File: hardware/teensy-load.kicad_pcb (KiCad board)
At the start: 2 copper layers, 43.2 x 59.1 mm, 19 parts, among them J101 Conn_01x02, J201 Conn_01x01_Male, Q201 BTS141, U101 TEENSY_4.0, U102 TLV4333, U201 DAC6571, U301 DAC6571

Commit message: After footprint check, before layout
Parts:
- added R201: 10K, Resistor_SMD:R_0805_2012Metric_Pad1.15x1.40mm_HandSolder, F.Cu at (118.7, 120.4)
- added R206: 10K, Resistor_SMD:R_0805_2012Metric_Pad1.15x1.40mm_HandSolder, F.Cu at (118.7, 123.3)
- added R207: 22K, Resistor_SMD:R_0805_2012Metric_Pad1.15x1.40mm_HandSolder, F.Cu at (123.5, 120.4)
- added R208: 220K, Resistor_SMD:R_0805_2012Metric_Pad1.15x1.40mm_HandSolder, F.Cu at (136.2, 114.6)
- added R303: 33K, Resistor_SMD:R_0805_2012Metric_Pad1.15x1.40mm_HandSolder, F.Cu at (133.2, 120.4)
- added R304: 27K, Resistor_SMD:R_0805_2012Metric_Pad1.15x1.40mm_HandSolder, F.Cu at (144.8, 114.6)
- added R305: 33K, Resistor_SMD:R_0805_2012Metric_Pad1.15x1.40mm_HandSolder, F.Cu at (138.0, 120.4)
- added R306: 39K, Resistor_SMD:R_0805_2012Metric_Pad1.15x1.40mm_HandSolder, F.Cu at (149.5, 114.6)
- R202: renamed from R201; value 23K -> 220K
- R203: renamed from R202; value 10K -> 22K
- R205: renamed from R204; value 0.1, 1W -> 10m, 3W
- R301: value 10K -> 39K
- R302: value 15K -> 27K
- R307: renamed from R303; value 9K -> 18K
- R308: renamed from R304; value 1K -> 2K
- moved J101 41.2 mm to (130.8, 45.1), turned to 180 degrees
- moved R205 5.24 mm to (135.9, 75.6), turned to 180 degrees
- renumbered R203 to R204
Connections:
- R302 pad 2: GND -> Net-(R302-Pad2)
- U102 pad 13: /Voltage control/V_SENSE -> Net-(R304-Pad1)
- U102 pad 6: /Current control/I_SENSE -> Net-(R206-Pad1)

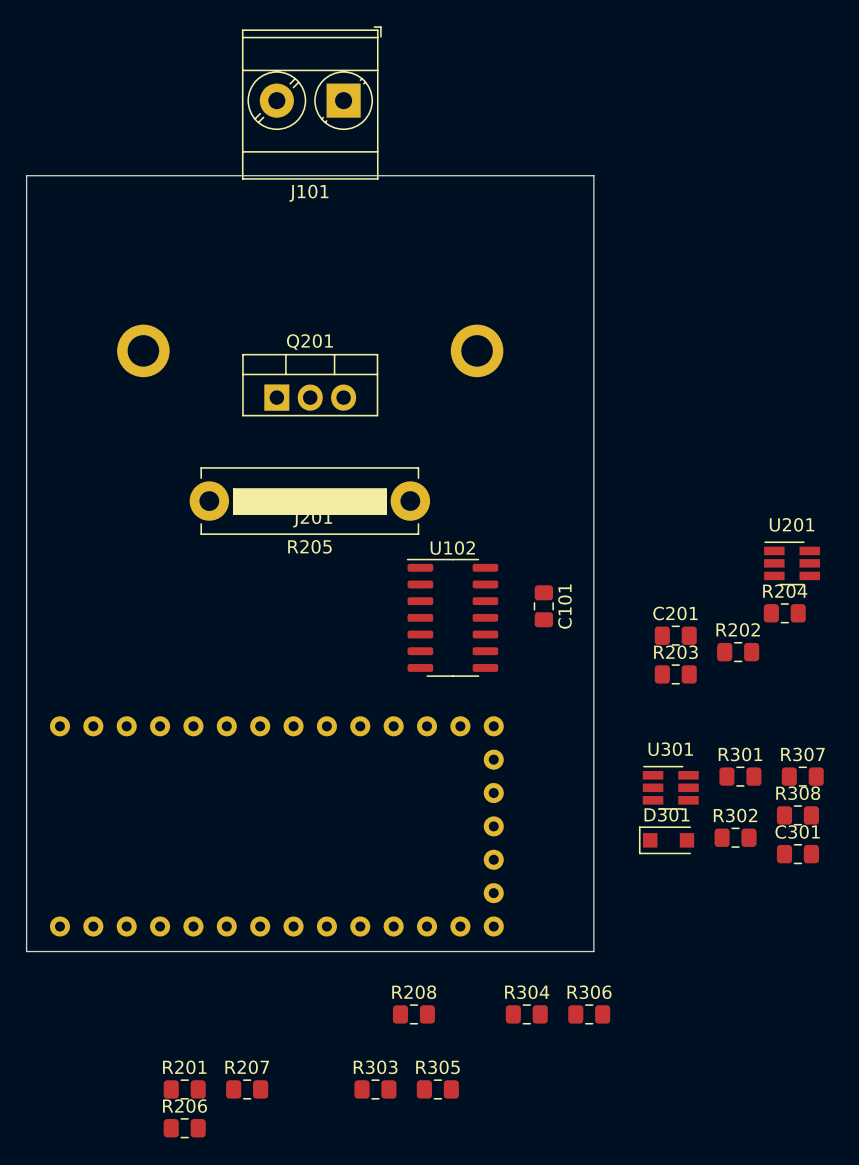
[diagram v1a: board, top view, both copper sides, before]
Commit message: Initial component placement
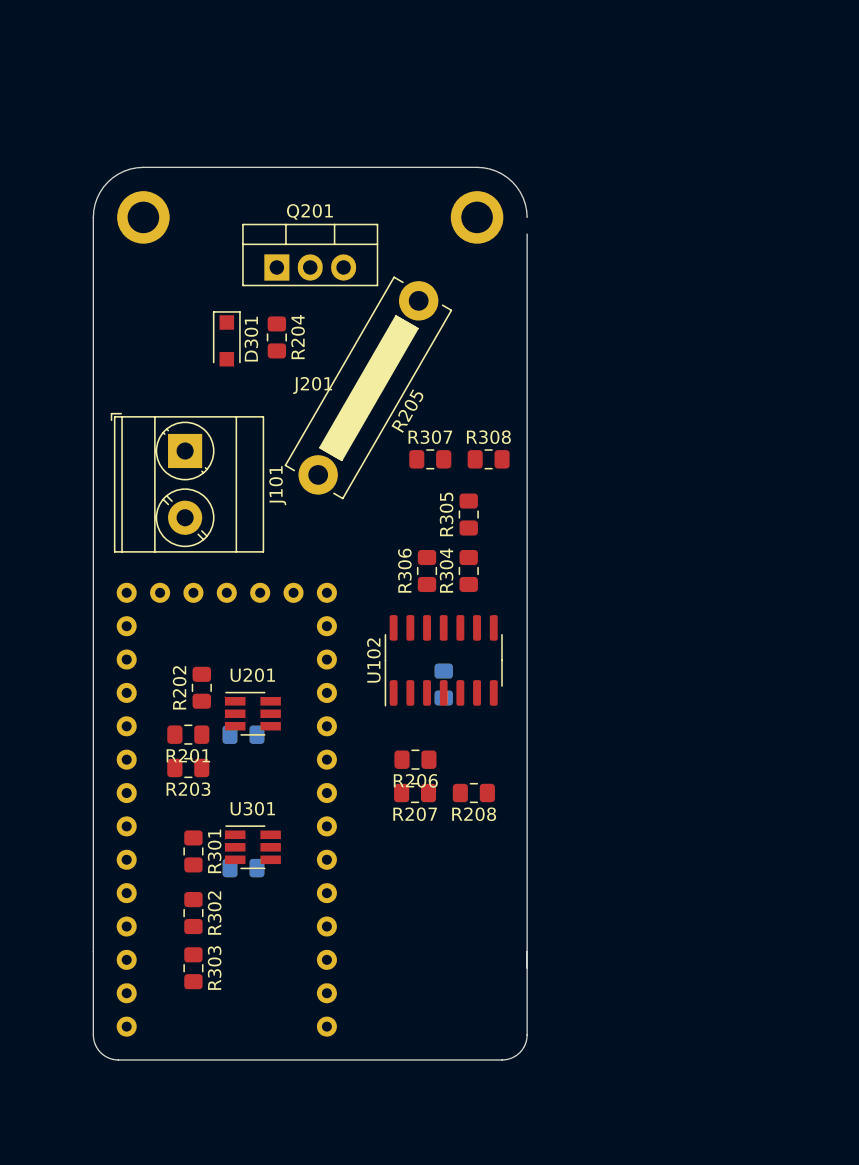
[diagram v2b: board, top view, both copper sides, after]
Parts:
- C101, C201, C301: moved to B.Cu
- moved D301 50.8 mm to (121.9, 63.4), turned to 270 degrees
- moved R204 44.0 mm to (125.7, 63.1), turned to 270 degrees
- moved R305 43.8 mm to (140.3, 76.6), turned to 90 degrees
- moved U201 42.6 mm to (123.9, 91.8)
- moved C301 42.2 mm to (123.2, 103.5)
- moved R301 42.0 mm to (119.4, 102.2), turned to 270 degrees
- moved R302 41.7 mm to (119.4, 106.9), turned to 270 degrees
- moved R202 40.9 mm to (120.0, 89.8), turned to 90 degrees
- moved R203 37.8 mm to (119.0, 95.9), turned to 180 degrees
- moved R307 37.2 mm to (137.4, 72.4)
- moved R306 35.9 mm to (137.2, 80.9), turned to 90 degrees
- moved R308 35.9 mm to (141.8, 72.4)
- moved R304 34.0 mm to (140.3, 80.9), turned to 90 degrees
- moved C201 33.8 mm to (123.2, 93.3)
- moved R206 33.1 mm to (136.3, 95.2), turned to 180 degrees
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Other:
- board size 43.2 x 59.1 mm -> 33 x 67.9 mm
- net class Default: clearance 0.2 -> 0.1524; trace_width 0.25 -> 0.1524; via_dia 0.8 -> 0.6858; via_drill 0.4 -> 0.3302
- rule pad_to_mask_clearance: 0.051 -> 0.0508
- rule solder_mask_min_width: 0.25 -> 0.1016
- rule trace_clearance: 0.2 -> 0.1524
- rule trace_min: 0.2 -> 0.1524
- rule via_min_drill: 0.3 -> 0.3302
- rule via_min_size: 0.4 -> 0.6858

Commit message: Layout done
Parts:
- moved J101 0.64 mm to (118.1, 71.8)
- moved R205 0.63 mm to (136.5, 61.0)
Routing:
- net Net-(R301-Pad2): track 0.00 -> 59.0 mm, vias 0 -> 4
- net /Current control/IN+: track 0.00 -> 48.9 mm
- net Net-(Q201-Pad3): track 0.00 -> 43.4 mm
- net GND: track 0.00 -> 42.1 mm, vias 0 -> 9
- net Net-(D301-Pad2): track 0.00 -> 36.2 mm, vias 0 -> 2
- net Net-(R204-Pad2): track 0.00 -> 29.7 mm
- net Net-(R201-Pad1): track 0.00 -> 28.8 mm
- net /Current control/I_SENSE: track 0.00 -> 23.5 mm, vias 0 -> 1
- net Net-(R307-Pad2): track 0.00 -> 22.3 mm
- net /Current control/I2C_SCL: track 0.00 -> 18.6 mm, vias 0 -> 1
- net /Current control/I2C_SDA: track 0.00 -> 15.3 mm
- net /Voltage control/V_SENSE: track 0.00 -> 14.0 mm, vias 0 -> 1
- net +3V3: track 0.00 -> 12.1 mm, vias 0 -> 3
- net Net-(R206-Pad1): track 0.00 -> 11.9 mm
- net /Current control/FET_GATE: track 0.00 -> 8.16 mm
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- added copper zone on F.Cu, net +3V3
- added copper zone on B.Cu, net GND
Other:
- outline, holes or cut-outs redrawn
- net class Default: trace_width 0.1524 -> 0.254
- net class High Current added: clearance 0.381, trace_width 1.905, via_dia 0.6858, via_drill 0.3302
- board text added: "Teensy Load V0.1 2020-04-22"
